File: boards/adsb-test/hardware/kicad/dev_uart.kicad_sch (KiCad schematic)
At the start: 38 parts, among them Q1701 MMBT3904, Q1702 MMBT3904, Q1703 MMBT3904, Q1704 MMBT3904, U1701 FT2232HL, U1702 93LC56B, U1703 74LVC1G07, U1704 74LVC1G125, U1705 74LVC1G07, U1706 74LVC1G125, Y1701 12MHz

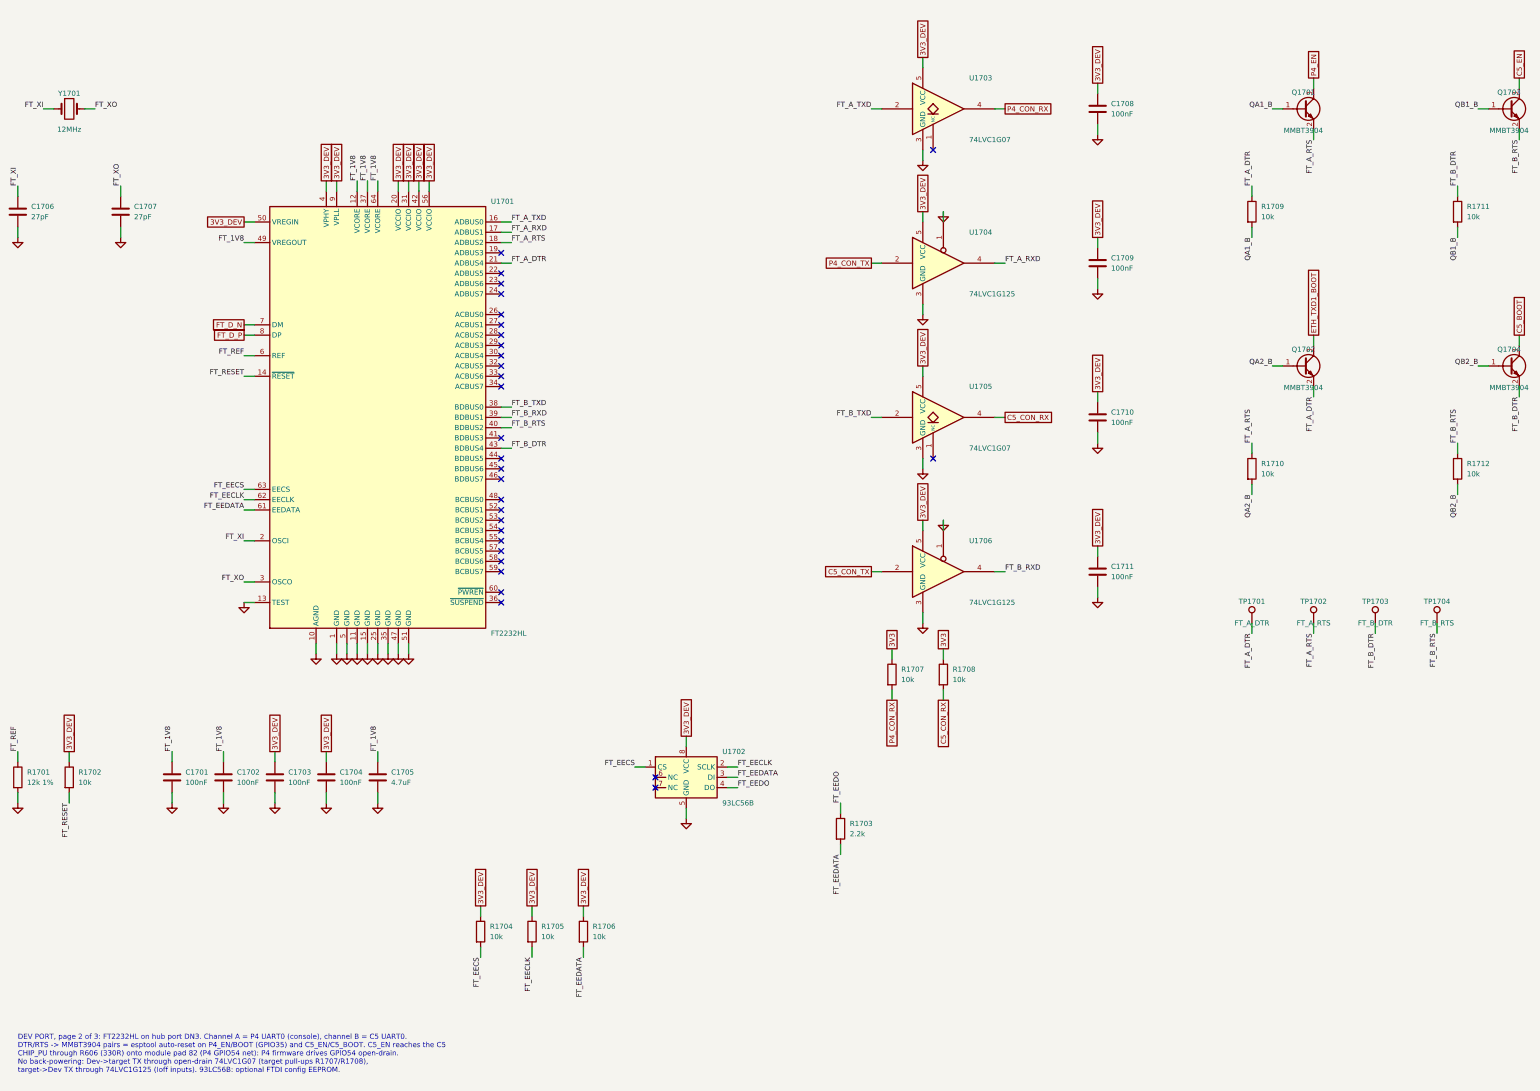
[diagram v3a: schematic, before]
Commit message: ADSB_Test: FT2232H spare port pins to DNP 2x10 headers J1701/J1702
All 16 pins of each FT2232H channel (xDBUS0-7 with the unused handshakes,
xCBUS0-7, 3V3_DEV, GND) on a not-fitted 2x10 header. ERC 0, PCB parity 0;
headers parked (commented in PLACE). Includes the user's placement edits.

Co-Authored-By: Claude Opus 5.5 <noreply@anthropic.com>
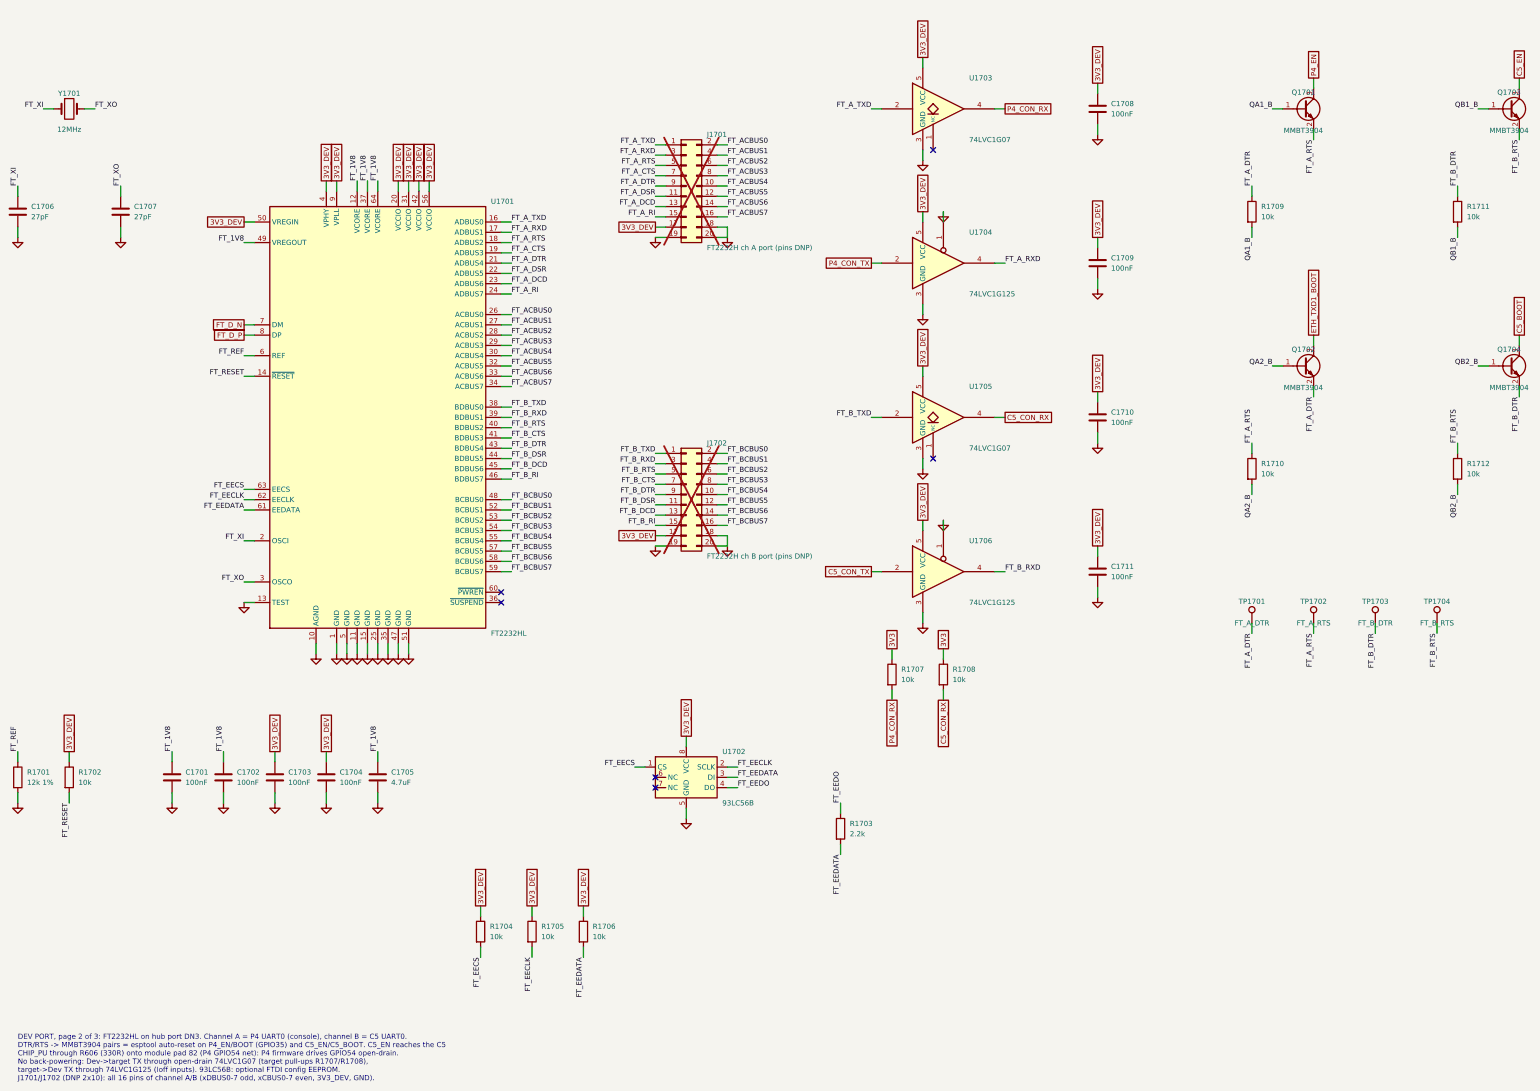
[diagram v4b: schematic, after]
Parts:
- added J1701: FT2232H ch A port (pins DNP), Connector_PinHeader_2.54mm:PinHeader_2x10_P2.54mm_Vertical, symbol Connector_Generic:Conn_02x10_Odd_Even
- added J1702: FT2232H ch B port (pins DNP), Connector_PinHeader_2.54mm:PinHeader_2x10_P2.54mm_Vertical, symbol Connector_Generic:Conn_02x10_Odd_Even
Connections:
- net 3V3_DEV: now also J1701.17 (Pin_17), J1702.17 (Pin_17)
- net FT_A_DTR: now also J1701.9 (Pin_9)
- net FT_A_RTS: now also J1701.5 (Pin_5)
- net FT_A_RXD: now also J1701.3 (Pin_3)
- net FT_A_TXD: now also J1701.1 (Pin_1)
- net FT_B_DTR: now also J1702.9 (Pin_9)
- net FT_B_RTS: now also J1702.5 (Pin_5)
- net FT_B_RXD: now also J1702.3 (Pin_3)
- net FT_B_TXD: now also J1702.1 (Pin_1)
- net GND: now also J1701.18 (Pin_18), J1701.19 (Pin_19), J1701.20 (Pin_20), J1702.18 (Pin_18), J1702.19 (Pin_19), J1702.20 (Pin_20)
- net FT_A_CTS: now reaches U1701.19 (ADBUS3)
- net FT_A_CTS: now also J1701.7 (Pin_7)
- net FT_A_DSR: now reaches U1701.22 (ADBUS5)
- net FT_A_DSR: now also J1701.11 (Pin_11)
- net FT_A_DCD: now reaches U1701.23 (ADBUS6)
- net FT_A_DCD: now also J1701.13 (Pin_13)
- net FT_A_RI: now reaches U1701.24 (ADBUS7)
- net FT_A_RI: now also J1701.15 (Pin_15)
- net FT_ACBUS0: now reaches U1701.26 (ACBUS0)
- net FT_ACBUS0: now also J1701.2 (Pin_2)
- net FT_ACBUS1: now reaches U1701.27 (ACBUS1)
- net FT_ACBUS1: now also J1701.4 (Pin_4)
- net FT_ACBUS2: now reaches U1701.28 (ACBUS2)
- net FT_ACBUS2: now also J1701.6 (Pin_6)
- net FT_ACBUS3: now reaches U1701.29 (ACBUS3)
- net FT_ACBUS3: now also J1701.8 (Pin_8)
- net FT_ACBUS4: now reaches U1701.30 (ACBUS4)
- net FT_ACBUS4: now also J1701.10 (Pin_10)
- net FT_ACBUS5: now reaches U1701.32 (ACBUS5)
- net FT_ACBUS5: now also J1701.12 (Pin_12)
- net FT_ACBUS6: now reaches U1701.33 (ACBUS6)
- net FT_ACBUS6: now also J1701.14 (Pin_14)
- net FT_ACBUS7: now reaches U1701.34 (ACBUS7)
- net FT_ACBUS7: now also J1701.16 (Pin_16)
- net FT_B_CTS: now reaches U1701.41 (BDBUS3)
- net FT_B_CTS: now also J1702.7 (Pin_7)
- net FT_B_DSR: now reaches U1701.44 (BDBUS5)
- net FT_B_DSR: now also J1702.11 (Pin_11)
- net FT_B_DCD: now reaches U1701.45 (BDBUS6)
- net FT_B_DCD: now also J1702.13 (Pin_13)
- net FT_B_RI: now reaches U1701.46 (BDBUS7)
- net FT_B_RI: now also J1702.15 (Pin_15)
- net FT_BCBUS0: now reaches U1701.48 (BCBUS0)
- net FT_BCBUS0: now also J1702.2 (Pin_2)
- net FT_BCBUS1: now reaches U1701.52 (BCBUS1)
- net FT_BCBUS1: now also J1702.4 (Pin_4)
- net FT_BCBUS2: now reaches U1701.53 (BCBUS2)
- net FT_BCBUS2: now also J1702.6 (Pin_6)
- net FT_BCBUS3: now reaches U1701.54 (BCBUS3)
- net FT_BCBUS3: now also J1702.8 (Pin_8)
- net FT_BCBUS4: now reaches U1701.55 (BCBUS4)
- net FT_BCBUS4: now also J1702.10 (Pin_10)
- net FT_BCBUS5: now reaches U1701.57 (BCBUS5)
- net FT_BCBUS5: now also J1702.12 (Pin_12)
- net FT_BCBUS6: now reaches U1701.58 (BCBUS6)
- net FT_BCBUS6: now also J1702.14 (Pin_14)
- net FT_BCBUS7: now reaches U1701.59 (BCBUS7)
- net FT_BCBUS7: now also J1702.16 (Pin_16)
- no-connect marks 30 -> 6
